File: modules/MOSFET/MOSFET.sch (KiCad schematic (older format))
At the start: 33 parts, among them J1 2, J10 11, J11 12, J12 13, J13 A0, J14 A1, J15 A2, J16 A3, J17 A4, J18 A5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

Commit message: Fix pin numbering to v2
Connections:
- net at J4.1 (Pin_1): now also Q2.1 (G), R2.1
- net at J5.1 (Pin_1): now also Q3.1 (G), R3.1
- now unconnected: J10.1 (Pin_1), J9.1 (Pin_1)
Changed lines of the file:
@@
 $EndComp
-Wire Wire Line
-	1225 3700 2000 3700
 Wire Wire Line
 	2000 3250 2750 3250
 Connection ~ 2750 3250
-Wire Wire Line
-	1225 3850 2000 3850
-Wire Wire Line
-	2000 4250 2750 4250
 Connection ~ 2750 4250
 $Comp
@@
 NoConn ~ 1225 2500
 NoConn ~ 1225 2800
-NoConn ~ 1225 2950
-NoConn ~ 1225 3100
 NoConn ~ 1225 3250
 NoConn ~ 1225 3400
@@
 NoConn ~ 6750 3250
 Wire Wire Line
-	2000 3250 2000 3700
+	1225 2950 2000 2950
 Wire Wire Line
-	2000 3850 2000 4250
+	2000 2950 2000 3250
+Wire Wire Line
+	1225 3100 1900 3100
+Wire Wire Line
+	1900 3100 1900 4250
+Wire Wire Line
+	1900 4250 2750 4250
+NoConn ~ 1225 3700
+NoConn ~ 1225 3850
 $EndSCHEMATC

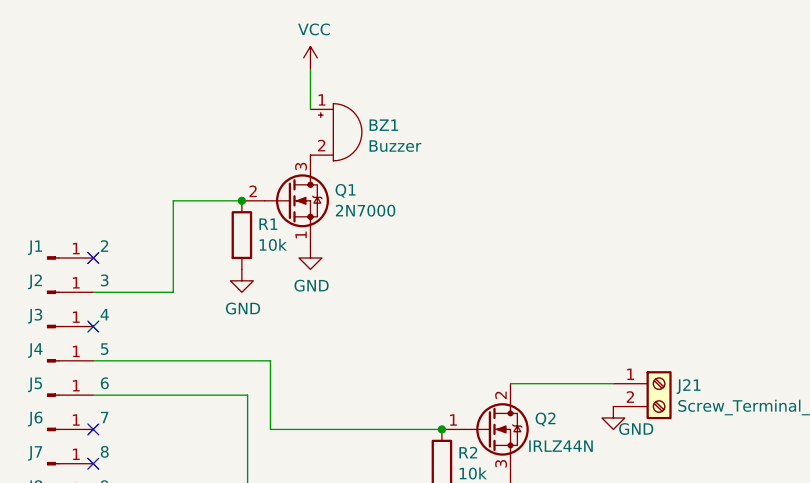
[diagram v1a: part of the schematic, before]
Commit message: MOSFET v2 pcb is ready. Change pin numbering. Add photomask.
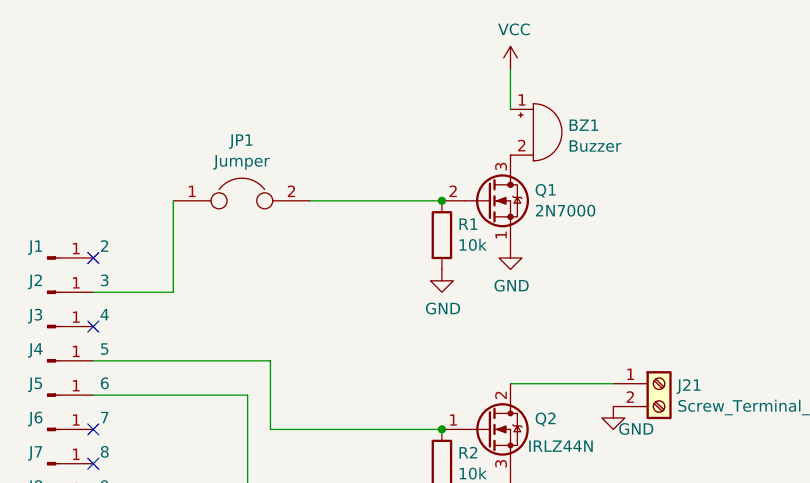
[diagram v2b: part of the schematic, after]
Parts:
- added JP1: Jumper, Connector_PinHeader_2.54mm:PinHeader_1x02_P2.54mm_Vertical, symbol Device:Jumper
- Q2, Q3: footprint Package_TO_SOT_THT:TO-220-3_Vertical -> Package_TO_SOT_THT:TO-220-3_Horizontal_TabDown
- R1, R2, R3: footprint Resistor_THT:R_Axial_DIN0207_L6.3mm_D2.5mm_P7.62mm_Horizontal -> Resistor_SMD:R_0805_2012Metric_Pad1.15x1.40mm_HandSolder
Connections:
- net at Q1.2 (G), R1.1: now also JP1.2; no longer J2.1 (Pin_1)
- new net: J2.1 (Pin_1), JP1.1
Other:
- moved on the sheet: BZ1, Q1, R1
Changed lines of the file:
@@
 F 0 "Q2" H 3156 3296 50  0000 L CNN
 F 1 "IRLZ44N" H 3125 3175 50  0000 L CNN
-F 2 "Package_TO_SOT_THT:TO-220-3_Vertical" H 3200 3175 50  0001 L CIN
+F 2 "Package_TO_SOT_THT:TO-220-3_Horizontal_TabDown" H 3200 3175 50  0001 L CIN
 F 3 "http://www.irf.com/product-info/datasheets/data/irlz44n.pdf" H 2950 3250 50  0001 L CNN
 	1    2950 3250
@@
 F 0 "R2" H 2820 3446 50  0000 L CNN
 F 1 "10k" H 2820 3355 50  0000 L CNN
-F 2 "Resistor_THT:R_Axial_DIN0207_L6.3mm_D2.5mm_P7.62mm_Horizontal" V 2680 3400 50  0001 C CNN
+F 2 "Resistor_SMD:R_0805_2012Metric_Pad1.15x1.40mm_HandSolder" V 2680 3400 50  0001 C CNN
 F 3 "~" H 2750 3400 50  0001 C CNN
 	1    2750 3400
@@
 F 0 "Q3" H 3156 4296 50  0000 L CNN
 F 1 "IRLZ44N" H 3125 4150 50  0000 L CNN
-F 2 "Package_TO_SOT_THT:TO-220-3_Vertical" H 3200 4175 50  0001 L CIN
+F 2 "Package_TO_SOT_THT:TO-220-3_Horizontal_TabDown" H 3200 4175 50  0001 L CIN
 F 3 "http://www.irf.com/product-info/datasheets/data/irlz44n.pdf" H 2950 4250 50  0001 L CNN
 	1    2950 4250
@@
 F 0 "R3" H 2820 4446 50  0000 L CNN
 F 1 "10k" H 2820 4355 50  0000 L CNN
-F 2 "Resistor_THT:R_Axial_DIN0207_L6.3mm_D2.5mm_P7.62mm_Horizontal" V 2680 4400 50  0001 C CNN
+F 2 "Resistor_SMD:R_0805_2012Metric_Pad1.15x1.40mm_HandSolder" V 2680 4400 50  0001 C CNN
 F 3 "~" H 2750 4400 50  0001 C CNN
 	1    2750 4400
@@
 L Device:Buzzer BZ1
 U 1 1 5E6C60BF
-P 2275 1950
-F 0 "BZ1" H 2427 1979 50  0000 L CNN
-F 1 "Buzzer" H 2427 1888 50  0000 L CNN
-F 2 "Buzzer_Beeper:Buzzer_12x9.5RM7.6" V 2250 2050 50  0001 C CNN
-F 3 "~" V 2250 2050 50  0001 C CNN
-	1    2275 1950
+P 3150 1950
+F 0 "BZ1" H 3302 1979 50  0000 L CNN
+F 1 "Buzzer" H 3302 1888 50  0000 L CNN
+F 2 "Buzzer_Beeper:Buzzer_12x9.5RM7.6" V 3125 2050 50  0001 C CNN
+F 3 "~" V 3125 2050 50  0001 C CNN
+	1    3150 1950
 	1    0    0    -1
 $EndComp
@@
 L Transistor_FET:2N7000 Q1
 U 1 1 5E6C7067
-P 2075 2250
-F 0 "Q1" H 2281 2296 50  0000 L CNN
-F 1 "2N7000" H 2281 2205 50  0000 L CNN
-F 2 "Package_TO_SOT_THT:TO-92_Inline" H 2275 2175 50  0001 L CIN
-F 3 "https://www.fairchildsemi.com/datasheets/2N/2N7000.pdf" H 2075 2250 50  0001 L CNN
-	1    2075 2250
+P 2950 2250
+F 0 "Q1" H 3156 2296 50  0000 L CNN
+F 1 "2N7000" H 3156 2205 50  0000 L CNN
+F 2 "Package_TO_SOT_THT:TO-92_Inline" H 3150 2175 50  0001 L CIN
+F 3 "https://www.fairchildsemi.com/datasheets/2N/2N7000.pdf" H 2950 2250 50  0001 L CNN
+	1    2950 2250
 	1    0    0    -1
 $EndComp
@@
 L Device:R R1
 U 1 1 5E6C8049
-P 1875 2400
-F 0 "R1" H 1945 2446 50  0000 L CNN
-F 1 "10k" H 1945 2355 50  0000 L CNN
-F 2 "Resistor_THT:R_Axial_DIN0207_L6.3mm_D2.5mm_P7.62mm_Horizontal" V 1805 2400 50  0001 C CNN
-F 3 "~" H 1875 2400 50  0001 C CNN
-	1    1875 2400
+P 2750 2400
+F 0 "R1" H 2820 2446 50  0000 L CNN
+F 1 "10k" H 2820 2355 50  0000 L CNN
+F 2 "Resistor_SMD:R_0805_2012Metric_Pad1.15x1.40mm_HandSolder" V 2680 2400 50  0001 C CNN
+F 3 "~" H 2750 2400 50  0001 C CNN
+	1    2750 2400
 	1    0    0    -1
 $EndComp
@@
 L power:GND #PWR01
 U 1 1 5E6C8660
-P 1875 2550
-F 0 "#PWR01" H 1875 2300 50  0001 C CNN
-F 1 "GND" H 1880 2377 50  0000 C CNN
-F 2 "" H 1875 2550 50  0001 C CNN
-F 3 "" H 1875 2550 50  0001 C CNN
-	1    1875 2550
+P 2750 2550
+F 0 "#PWR01" H 2750 2300 50  0001 C CNN
+F 1 "GND" H 2755 2377 50  0000 C CNN
+F 2 "" H 2750 2550 50  0001 C CNN
+F 3 "" H 2750 2550 50  0001 C CNN
+	1    2750 2550
 	1    0    0    -1
 $EndComp
@@
 L power:VCC #PWR02
 U 1 1 5E6C8E12
-P 2175 1675
-F 0 "#PWR02" H 2175 1525 50  0001 C CNN
-F 1 "VCC" H 2192 1848 50  0000 C CNN
-F 2 "" H 2175 1675 50  0001 C CNN
-F 3 "" H 2175 1675 50  0001 C CNN
-	1    2175 1675
-	1    0    0    -1
-$EndComp
-Wire Wire Line
-	2175 1675 2175 1850
+P 3050 1675
+F 0 "#PWR02" H 3050 1525 50  0001 C CNN
+F 1 "VCC" H 3067 1848 50  0000 C CNN
+F 2 "" H 3050 1675 50  0001 C CNN
+F 3 "" H 3050 1675 50  0001 C CNN
+	1    3050 1675
+	1    0    0    -1
+$EndComp
+Wire Wire Line
+	3050 1675 3050 1850
 Wire Wire Line
 	1225 2650 1575 2650
 Wire Wire Line
 	1575 2650 1575 2250
-Wire Wire Line
-	1575 2250 1875 2250
-Connection ~ 1875 2250
+Connection ~ 2750 2250
 $Comp
 L power:GND #PWR03
 U 1 1 5E6CA0D8
-P 2175 2450
-F 0 "#PWR03" H 2175 2200 50  0001 C CNN
-F 1 "GND" H 2180 2277 50  0000 C CNN
-F 2 "" H 2175 2450 50  0001 C CNN
-F 3 "" H 2175 2450 50  0001 C CNN
-	1    2175 2450
+P 3050 2450
+F 0 "#PWR03" H 3050 2200 50  0001 C CNN
+F 1 "GND" H 3055 2277 50  0000 C CNN
+F 2 "" H 3050 2450 50  0001 C CNN
+F 3 "" H 3050 2450 50  0001 C CNN
+	1    3050 2450
 	1    0    0    -1
 $EndComp
@@
 NoConn ~ 1225 3700
 NoConn ~ 1225 3850
+$Comp
+L Device:Jumper JP1
+U 1 1 5E9A4017
+P 1875 2250
+F 0 "JP1" H 1875 2514 50  0000 C CNN
+F 1 "Jumper" H 1875 2423 50  0000 C CNN
+F 2 "Connector_PinHeader_2.54mm:PinHeader_1x02_P2.54mm_Vertical" H 1875 2250 50  0001 C CNN
+F 3 "~" H 1875 2250 50  0001 C CNN
+	1    1875 2250
+	1    0    0    -1
+$EndComp
+Wire Wire Line
+	2175 2250 2750 2250
 $EndSCHEMATC

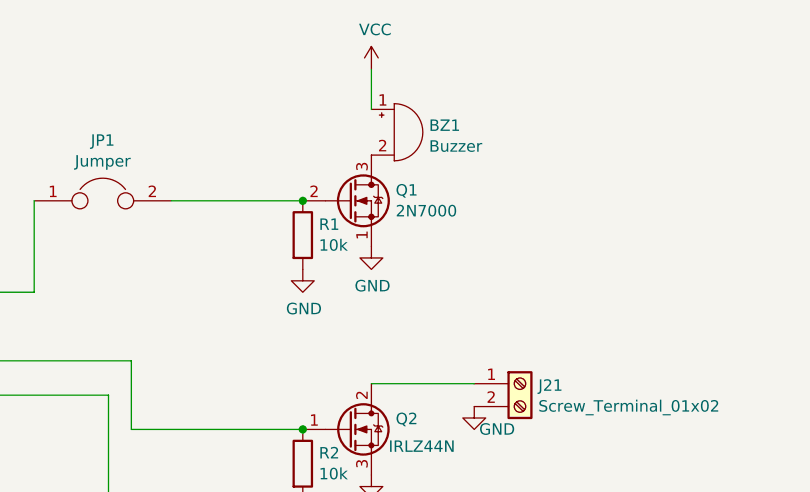
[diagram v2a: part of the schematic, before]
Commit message: Replace 2N7000 -> IRLML
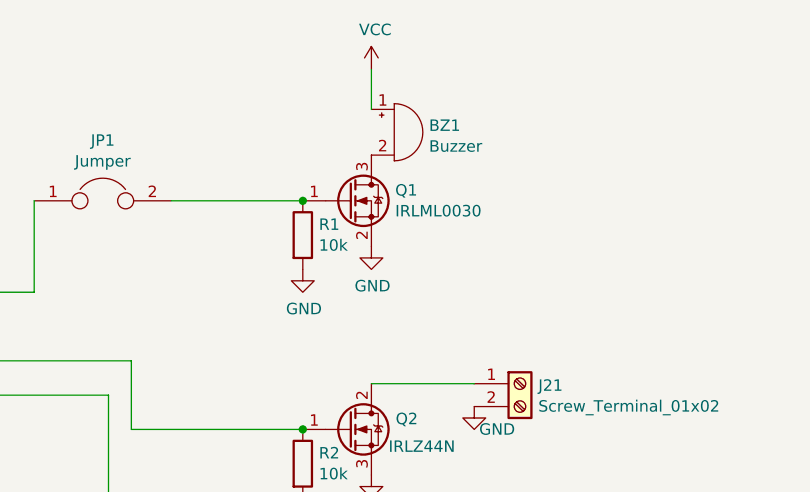
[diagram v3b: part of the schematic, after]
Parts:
- removed Q1: 2N7000, Package_TO_SOT_THT:TO-92_Inline, symbol Transistor_FET:2N7000
- added Q1: IRLML0030, Package_TO_SOT_SMD:SOT-23, symbol Transistor_FET:IRLML0030
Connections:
- net GND: now also Q1.2 (S)
- net at BZ1.2 (+): now also Q1.3 (D)
- net at JP1.2, R1.1: now also Q1.1 (G)
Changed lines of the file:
@@
 EESchema Schematic File Version 4
-LIBS:MOSFET-cache
 EELAYER 30 0
 EELAYER END
@@
 $EndComp
 $Comp
-L Transistor_FET:2N7000 Q1
-U 1 1 5E6C7067
-P 2950 2250
-F 0 "Q1" H 3156 2296 50  0000 L CNN
-F 1 "2N7000" H 3156 2205 50  0000 L CNN
-F 2 "Package_TO_SOT_THT:TO-92_Inline" H 3150 2175 50  0001 L CIN
-F 3 "https://www.fairchildsemi.com/datasheets/2N/2N7000.pdf" H 2950 2250 50  0001 L CNN
-	1    2950 2250
-	1    0    0    -1
-$EndComp
-$Comp
 L Device:R R1
 U 1 1 5E6C8049
@@
 Wire Wire Line
 	1575 2650 1575 2250
-Connection ~ 2750 2250
 $Comp
 L power:GND #PWR03
@@
 Wire Wire Line
 	2175 2250 2750 2250
+$Comp
+L Transistor_FET:IRLML0030 Q1
+U 1 1 5FA73B7C
+P 2950 2250
+F 0 "Q1" H 3154 2296 50  0000 L CNN
+F 1 "IRLML0030" H 3154 2205 50  0000 L CNN
+F 2 "Package_TO_SOT_SMD:SOT-23" H 3150 2175 50  0001 L CIN
+F 3 "https://www.infineon.com/dgdl/irlml0030pbf.pdf?fileId=5546d462533600a401535664773825df" H 2950 2250 50  0001 L CNN
+	1    2950 2250
+	1    0    0    -1
+$EndComp
+Connection ~ 2750 2250
 $EndSCHEMATC
